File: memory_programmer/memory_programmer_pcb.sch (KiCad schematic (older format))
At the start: 13 parts, among them J1 Conn_01x03, P1 Power, P2 Analog, P3 Digital, P4 Digital, P5 CONN_01X01, P6 CONN_01X01, P7 CONN_01X01, P8 CONN_01X01

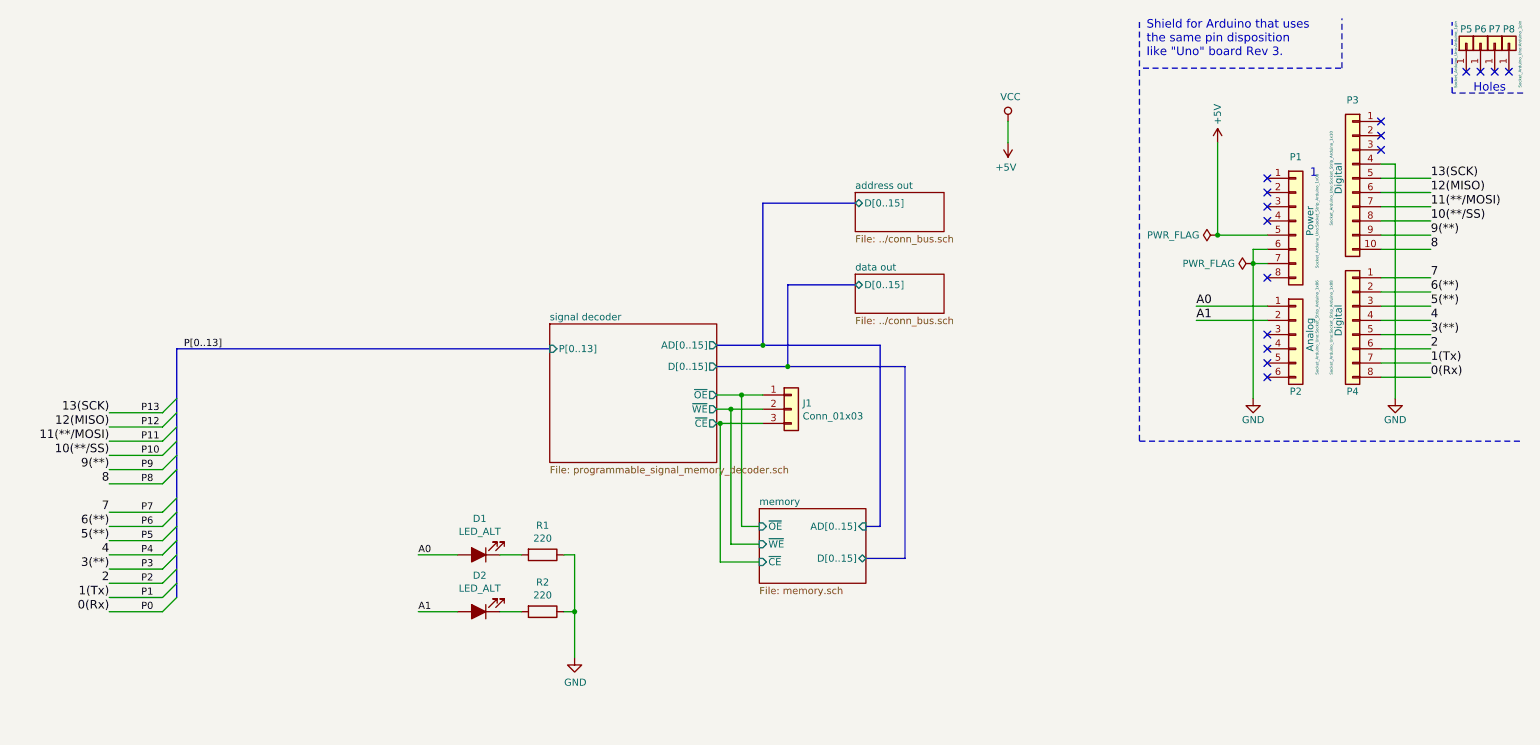
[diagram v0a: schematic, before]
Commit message: memory programmer and cu
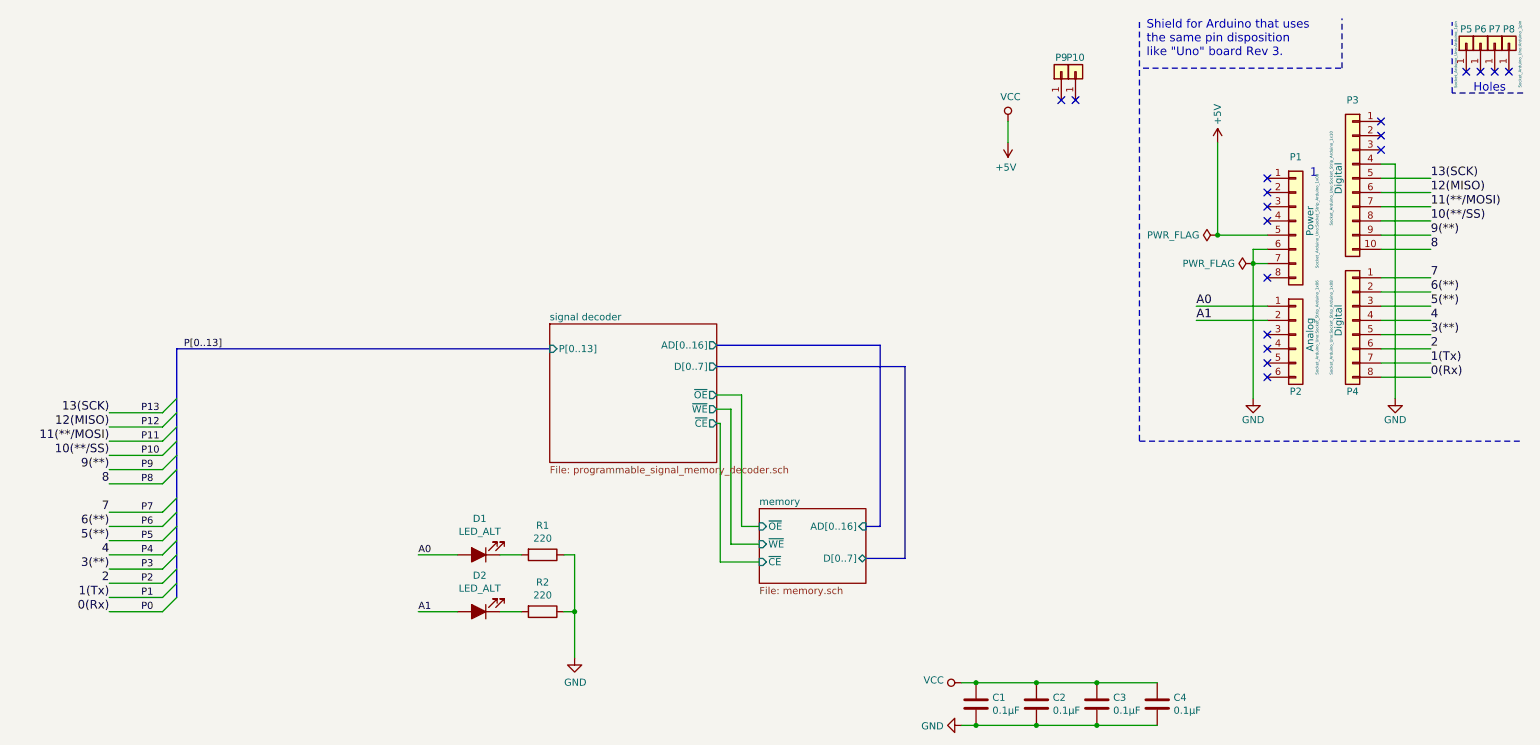
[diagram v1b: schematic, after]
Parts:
- removed J1: Conn_01x03, Connector_PinHeader_2.54mm:PinHeader_1x03_P2.54mm_Vertical, symbol Connector_Generic:Conn_01x03
- added C1, C2, C3, C4: 0.1µF, Capacitor_THT:C_Disc_D4.3mm_W1.9mm_P5.00mm, symbol Device:C
- added P10, P9: CONN_01X01, Socket_Arduino_Uno:Arduino_1pin, symbol Connector_Generic:Conn_01x01
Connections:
- net +5V: now also C1.2, C2.2, C3.2, C4.2
- net GND: now also C1.1, C2.1, C3.1, C4.1
- no-connect marks 16 -> 18
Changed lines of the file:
@@
 $Descr A4 11693 8268
 encoding utf-8
-Sheet 1 5
+Sheet 1 3
 Title ""
 Date "lun. 30 mars 2015"
@@
 	10700 1000 10700 500
 $Sheet
-S 6500 2275 625  275
-U 5EE115FB
-F0 "data out" 50
-F1 "../conn_bus.sch" 50
-F2 "D[0..15]" B L 6500 2350 50
-$EndSheet
-$Sheet
-S 6500 1700 625  275
-U 5EE11E3D
-F0 "address out" 50
-F1 "../conn_bus.sch" 50
-F2 "D[0..15]" B L 6500 1775 50
-$EndSheet
-Wire Bus Line
-	5525 2775 5850 2775
-Wire Bus Line
-	5850 2775 5850 1775
-Wire Bus Line
-	5850 1775 6500 1775
-Wire Bus Line
-	5525 2925 6025 2925
-Wire Bus Line
-	6025 2925 6025 2350
-Wire Bus Line
-	6025 2350 6500 2350
-$Sheet
 S 5825 3925 750  525
 U 5EE1C593
 F0 "memory" 50
 F1 "memory.sch" 50
-F2 "AD[0..15]" I R 6575 4050 50
-F3 "D[0..15]" B R 6575 4275 50
+F2 "AD[0..16]" I R 6575 4050 50
+F3 "D[0..7]" B R 6575 4275 50
 F4 "~WE~" I L 5825 4175 50
 F5 "~CE~" I L 5825 4300 50
@@
 Wire Wire Line
 	5525 3125 5700 3125
-$Comp
-L Connector_Generic:Conn_01x03 J1
-U 1 1 5EE16863
-P 6050 3225
-F 0 "J1" H 6130 3267 50  0000 L CNN
-F 1 "Conn_01x03" H 6130 3176 50  0000 L CNN
-F 2 "Connector_PinHeader_2.54mm:PinHeader_1x03_P2.54mm_Vertical" H 6050 3225 50  0001 C CNN
-F 3 "~" H 6050 3225 50  0001 C CNN
-	1    6050 3225
-	1    0    0    -1
-$EndComp
 Wire Wire Line
 	5825 4050 5700 4050
 Wire Wire Line
 	5700 4050 5700 3125
-Connection ~ 5700 3125
-Wire Wire Line
-	5700 3125 5850 3125
 Wire Wire Line
 	5625 3225 5625 4175
 Wire Wire Line
 	5625 4175 5825 4175
-Connection ~ 5625 3225
-Wire Wire Line
-	5625 3225 5850 3225
 Wire Wire Line
 	5825 4300 5550 4300
 Wire Wire Line
 	5550 4300 5550 3325
-Connection ~ 5550 3325
-Wire Wire Line
-	5550 3325 5850 3325
 Wire Bus Line
 	6575 4275 6850 4275
@@
 	6850 4275 6850 2925
 Wire Bus Line
-	6850 2925 6025 2925
-Connection ~ 6025 2925
-Wire Bus Line
 	6575 4050 6675 4050
 Wire Bus Line
 	6675 4050 6675 2775
-Wire Bus Line
-	6675 2775 5850 2775
-Connection ~ 5850 2775
 $Comp
 L Device:LED_ALT D2
@@
 Wire Bus Line
 	1725 2800 4350 2800
-$Sheet
-S 4350 2625 1175 975
-U 5EDF08FE
-F0 "signal decoder" 50
-F1 "programmable_signal_memory_decoder.sch" 50
-F2 "P[0..13]" I L 4350 2800 50
-F3 "AD[0..15]" O R 5525 2775 50
-F4 "D[0..15]" O R 5525 2925 50
-F5 "~OE~" O R 5525 3125 50
-F6 "~WE~" O R 5525 3225 50
-F7 "~CE~" O R 5525 3325 50
-$EndSheet
 Wire Wire Line
 	9300 2200 9300 3150
@@
 	0    -1   -1   0
 $EndComp
-Wire Bus Line
-	1725 2800 1725 4550
 Wire Wire Line
 	9300 2100 9300 2200
 Connection ~ 9050 2000
+Wire Bus Line
+	5525 2925 6850 2925
+Wire Bus Line
+	5525 2775 6675 2775
+$Sheet
+S 4350 2625 1175 975
+U 5EDF08FE
+F0 "signal decoder" 50
+F1 "programmable_signal_memory_decoder.sch" 50
+F2 "P[0..13]" I L 4350 2800 50
+F3 "AD[0..16]" O R 5525 2775 50
+F4 "D[0..7]" O R 5525 2925 50
+F5 "~OE~" O R 5525 3125 50
+F6 "~WE~" O R 5525 3225 50
+F7 "~CE~" O R 5525 3325 50
+$EndSheet
+$Comp
+L Device:C C1
+U 1 1 5F5AC9FC
+P 7350 5300
+F 0 "C1" H 7235 5254 50  0000 R CNN
+F 1 "0.1µF" H 7235 5345 50  0000 R CNN
+F 2 "Capacitor_THT:C_Disc_D4.3mm_W1.9mm_P5.00mm" H 7388 5150 50  0001 C CNN
+F 3 "~" H 7350 5300 50  0001 C CNN
+	1    7350 5300
+	-1   0    0    1
+$EndComp
+$Comp
+L Device:C C2
+U 1 1 5F5ADA6D
+P 7775 5300
+F 0 "C2" H 7660 5254 50  0000 R CNN
+F 1 "0.1µF" H 7660 5345 50  0000 R CNN
+F 2 "Capacitor_THT:C_Disc_D4.3mm_W1.9mm_P5.00mm" H 7813 5150 50  0001 C CNN
+F 3 "~" H 7775 5300 50  0001 C CNN
+	1    7775 5300
+	-1   0    0    1
+$EndComp
+$Comp
+L Device:C C3
+U 1 1 5F5AF00E
+P 8200 5300
+F 0 "C3" H 8085 5254 50  0000 R CNN
+F 1 "0.1µF" H 8085 5345 50  0000 R CNN
+F 2 "Capacitor_THT:C_Disc_D4.3mm_W1.9mm_P5.00mm" H 8238 5150 50  0001 C CNN
+F 3 "~" H 8200 5300 50  0001 C CNN
+	1    8200 5300
+	-1   0    0    1
+$EndComp
+$Comp
+L Device:C C4
+U 1 1 5F5B07EE
+P 8625 5300
+F 0 "C4" H 8510 5254 50  0000 R CNN
+F 1 "0.1µF" H 8510 5345 50  0000 R CNN
+F 2 "Capacitor_THT:C_Disc_D4.3mm_W1.9mm_P5.00mm" H 8663 5150 50  0001 C CNN
+F 3 "~" H 8625 5300 50  0001 C CNN
+	1    8625 5300
+	-1   0    0    1
+$EndComp
+Wire Wire Line
+	8625 5150 8200 5150
+Connection ~ 7350 5150
+Wire Wire Line
+	7350 5150 7250 5150
+Connection ~ 7775 5150
+Wire Wire Line
+	7775 5150 7350 5150
+Connection ~ 8200 5150
+Wire Wire Line
+	8200 5150 7775 5150
+Wire Wire Line
+	8625 5450 8200 5450
+Connection ~ 7350 5450
+Wire Wire Line
+	7350 5450 7250 5450
+Connection ~ 7775 5450
+Wire Wire Line
+	7775 5450 7350 5450
+Connection ~ 8200 5450
+Wire Wire Line
+	8200 5450 7775 5450
+$Comp
+L power:GND #PWR0102
+U 1 1 5F5B6745
+P 7250 5450
+F 0 "#PWR0102" H 7250 5200 50  0001 C CNN
+F 1 "GND" V 7255 5322 50  0000 R CNN
+F 2 "" H 7250 5450 50  0001 C CNN
+F 3 "" H 7250 5450 50  0001 C CNN
+	1    7250 5450
+	0    1    1    0
+$EndComp
+$Comp
+L power:VCC #PWR0103
+U 1 1 5F5B6A54
+P 7250 5150
+F 0 "#PWR0103" H 7250 5000 50  0001 C CNN
+F 1 "VCC" V 7268 5277 50  0000 L CNN
+F 2 "" H 7250 5150 50  0001 C CNN
+F 3 "" H 7250 5150 50  0001 C CNN
+	1    7250 5150
+	0    -1   -1   0
+$EndComp
+$Comp
+L Connector_Generic:Conn_01x01 P9
+U 1 1 5F47462B
+P 7950 850
+F 0 "P9" V 8050 850 50  0000 C CNN
+F 1 "CONN_01X01" V 8050 850 50  0001 C CNN
+F 2 "Socket_Arduino_Uno:Arduino_1pin" H 7950 850 20  0001 C CNN
+F 3 "" H 7950 850 50  0000 C CNN
+	1    7950 850
+	0    -1   -1   0
+$EndComp
+$Comp
+L Connector_Generic:Conn_01x01 P10
+U 1 1 5F474631
+P 8050 850
+F 0 "P10" V 8150 850 50  0000 C CNN
+F 1 "CONN_01X01" V 8150 850 50  0001 C CNN
+F 2 "Socket_Arduino_Uno:Arduino_1pin" V 8050 850 20  0001 C CNN
+F 3 "" H 8050 850 50  0000 C CNN
+	1    8050 850
+	0    -1   -1   0
+$EndComp
+NoConn ~ 7950 1050
+NoConn ~ 8050 1050
+Wire Bus Line
+	1725 2800 1725 4550
 $EndSCHEMATC
